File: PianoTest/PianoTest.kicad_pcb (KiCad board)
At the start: 4 copper layers, 120 x 90 mm, 199 parts, among them J101 SMA preampl., J102 SMA shaper, J301 TRIG est., J401 J_IN MAIN, J402 J_OUT MAIN, Q101 BF862, Q102 BF862, Q301 BSS138, U101 OPA4172ID, U102 ADS8326IDGKT, U103 TMP117AIDRVR, U201 MCP23S17-E/ML, U202 TMUX1112RSVR, U203 TMUX1112RSVR, U204 BGSA142GN12, U205 BGSA142GN12, U301 LTC6993CS6-2, U302 AD5245BRJZ100, U401 74HC283, U402 74HC85, U403 74HC138, U404 SN74LVC2G17DBVR, U405 SN74LVC1G125DBVR, U406 SN74LVC1G332DBVR, U407 SN74LVC1G07DBVR, U408 25AA02E48T-I/SN, U501 DAC61402RHBR, U502 INA239AIDGSR

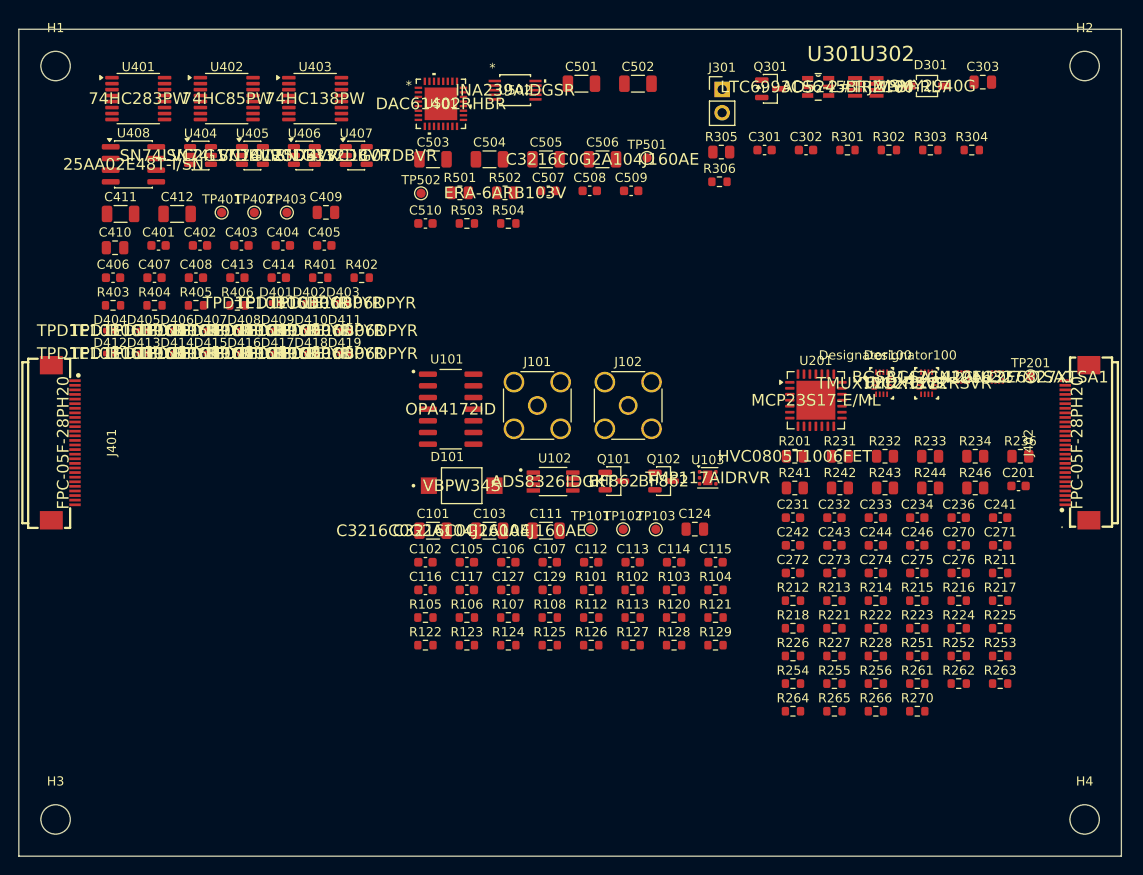
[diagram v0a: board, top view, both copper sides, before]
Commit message: PianoTest: discriminatore, latch e rilevatore di picco
Comparatore TLV3501 su SHAPER_OUT con soglia dal canale B del DAC61402
(partitore 22k/10k, BAT54S), latch 74LVC1G74 su GPA7 dell'MCP (ALERT#),
uscita HIT su TP e SMA. Rilevatore di picco OPA2365 + BAS416 + hold 1 nF
C0G prima dell'ADS8326, con reset da accesso SPI all'indirizzo 3 e
ponticello 0R per scavalcarlo. Trigger del LED dallo strobe dell'indirizzo 4.
Articolo: sezione 3.1 (formatore e acquisizione) aggiornata e ricompilata.
ERC 0.

Co-Authored-By: Claude Opus 5.5 (1M context) <noreply@anthropic.com>
Claude-Session: https://claude.ai/code/session_01J3krgWFTUEjwvCnwUp9cQn
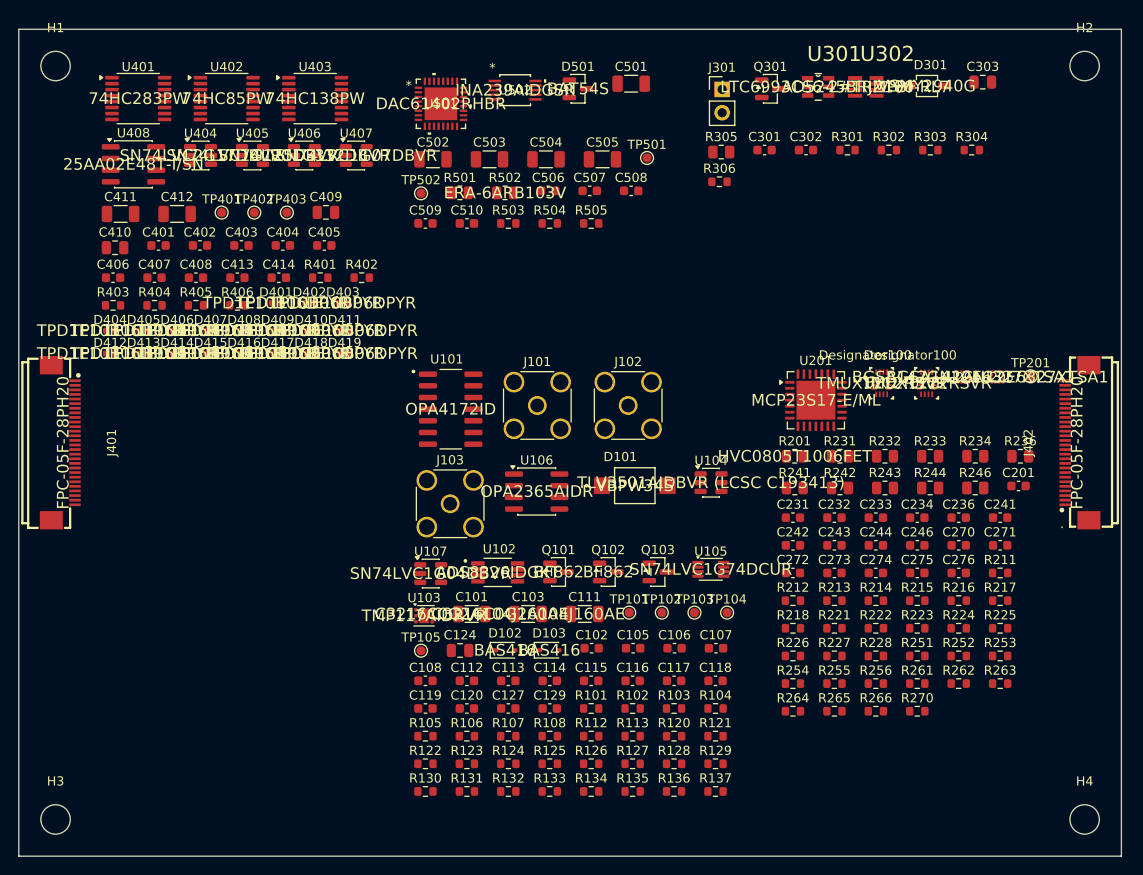
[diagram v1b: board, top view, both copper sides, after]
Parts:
- added C108: 1nF C0G, Capacitor_SMD:C_0603_1608Metric, F.Cu at (84.3, 110.9)
- added C118: 100nF, Capacitor_SMD:C_0603_1608Metric, F.Cu at (115.8, 110.9)
- added C119: 100nF, Capacitor_SMD:C_0603_1608Metric, F.Cu at (84.3, 113.9)
- added C120: 100nF, Capacitor_SMD:C_0603_1608Metric, F.Cu at (88.8, 113.9)
- added D102: BAS416, Diode_SMD:D_SOD-323, F.Cu at (92.9, 107.6)
- added D103: BAS416, Diode_SMD:D_SOD-323, F.Cu at (97.7, 107.6)
- added D501: BAT54S, Package_TO_SOT_SMD:SOT-23, F.Cu at (100.9, 46.5)
- added J103: SMA HIT, Connector_Coaxial:SMA_Amphenol_132134_Vertical, F.Cu at (86.9, 91.6)
- added Q103: BSS138, Package_TO_SOT_SMD:SOT-23, F.Cu at (109.6, 99.1)
- added R130: 1k, Resistor_SMD:R_0603_1608Metric, F.Cu at (84.3, 123.0)
- added R131: 1M, Resistor_SMD:R_0603_1608Metric, F.Cu at (88.8, 123.0)
- added R132: 1k, Resistor_SMD:R_0603_1608Metric, F.Cu at (93.3, 123.0)
- added R133: 10k, Resistor_SMD:R_0603_1608Metric, F.Cu at (97.8, 123.0)
- added R134: 100k, Resistor_SMD:R_0603_1608Metric, F.Cu at (102.3, 123.0)
- added R135: 0R, Resistor_SMD:R_0603_1608Metric, F.Cu at (106.8, 123.0)
- added R136: 0R, Resistor_SMD:R_0603_1608Metric, F.Cu at (111.3, 123.0)
- added R137: 100R, Resistor_SMD:R_0603_1608Metric, F.Cu at (115.8, 123.0)
- added R505: 10k, Resistor_SMD:R_0603_1608Metric, F.Cu at (102.3, 61.1)
- added TP104: HIT, TestPoint:TestPoint_Pad_D1.0mm, F.Cu at (117.1, 103.5)
- added TP105: PK_OUT, TestPoint:TestPoint_Pad_D1.0mm, F.Cu at (83.8, 107.6)
- added U104: TLV3501AIDBVR, Package_TO_SOT_SMD:SOT-23-6, F.Cu at (115.3, 89.3)
- added U105: SN74LVC1G74DCUR, Package_SO:VSSOP-8_2.3x2mm_P0.5mm, F.Cu at (115.3, 98.8)
- added U106: OPA2365AIDR, Package_SO:SOIC-8_3.9x4.9mm_P1.27mm, F.Cu at (96.4, 90.3)
- added U107: SN74LVC1G04DBVR, Package_TO_SOT_SMD:SOT-23-5, F.Cu at (84.8, 99.2)
- C506: value 100nF/100V C0G -> 100nF; footprint Capacitor_SMD:C_1206_3216Metric -> Capacitor_SMD:C_0603_1608Metric
- R503: value 1k -> 22k
- TP502: value VBIAS_B -> VTH
- moved U103 34.3 mm to (84.1, 103.8)
- moved C124 28.8 mm to (88.0, 107.6)
- moved C117 24.6 mm to (111.3, 110.9)
- moved C116 24.6 mm to (106.8, 110.9)
- moved C502 23.8 mm to (85.1, 54.2)
- moved C509 22.7 mm to (84.3, 61.1)
- moved C102 20.4 mm to (102.3, 107.4)
- moved C105 20.4 mm to (106.9, 107.4)
- moved C107 20.4 mm to (115.9, 107.4)
- moved C106 20.4 mm to (111.4, 107.4)
- moved D101 18.8 mm to (107.0, 89.7)
- moved C115 18.7 mm to (102.3, 110.9)
- moved C114 18.7 mm to (97.8, 110.9)
- moved C112 18.7 mm to (88.8, 110.9)
- moved C113 18.7 mm to (93.3, 110.9)
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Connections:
- net /BiasDiodo/VBIAS_B renamed VTH
- net /bus-pnp/CS_Y3 renamed CS_Y3
- R106 pad 1: /Rivelatore/SHAPER_OUT -> /Rivelatore/ADC_SRC
- R304 pad 1: TRIG_MCP -> CS_Y4
- TP402 pad 1: /bus-pnp/CS_Y4 -> CS_Y4
- U201 pad 24: TRIG_MCP -> HIT_LATCH
- U403 pad 11: /bus-pnp/CS_Y4 -> CS_Y4

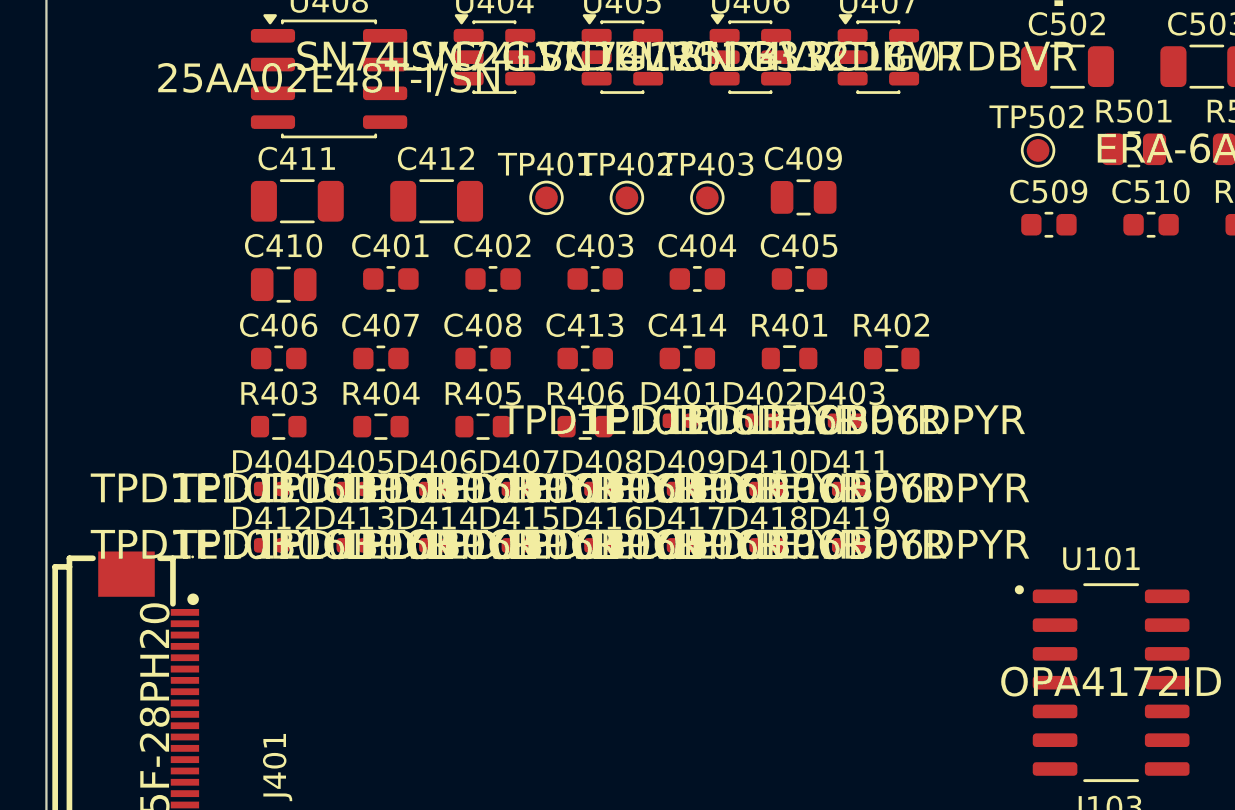
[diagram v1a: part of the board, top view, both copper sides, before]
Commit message: Bus MIKILAB REV5.1: linea di coincidenza HIT# sul pin 28 del MAIN
Specifica: pin 28 (prima GND ridondante) = HIT#, open-drain attivo basso,
pull-up unico 4.7k sul master, impulso 100-200 ns per evento; logica di
coincidenza documentata (fronte marcato dal master, lettura dei latch).
PianoTest: HIT -> monostabile 74LVC1G123 (2k + 27 pF) -> 74LVC1G06 su
HIT#, passante J_IN -> J_OUT, ESD. ERC 0.
SchedaA133: J2 pin 28 -> PD4 (PD_EINT4), pull-up R336 4.7k, ESD su U307,
R337 0R DNP verso l'EXTINT del NEO-F10T. ERC 0, PDF rigenerato.
Documentazione bus della A133 e articolo (sezione bus e coincidenze)
aggiornati; corretta l'identita del primo piano (0).

Co-Authored-By: Claude Opus 5.5 (1M context) <noreply@anthropic.com>
Claude-Session: https://claude.ai/code/session_01J3krgWFTUEjwvCnwUp9cQn
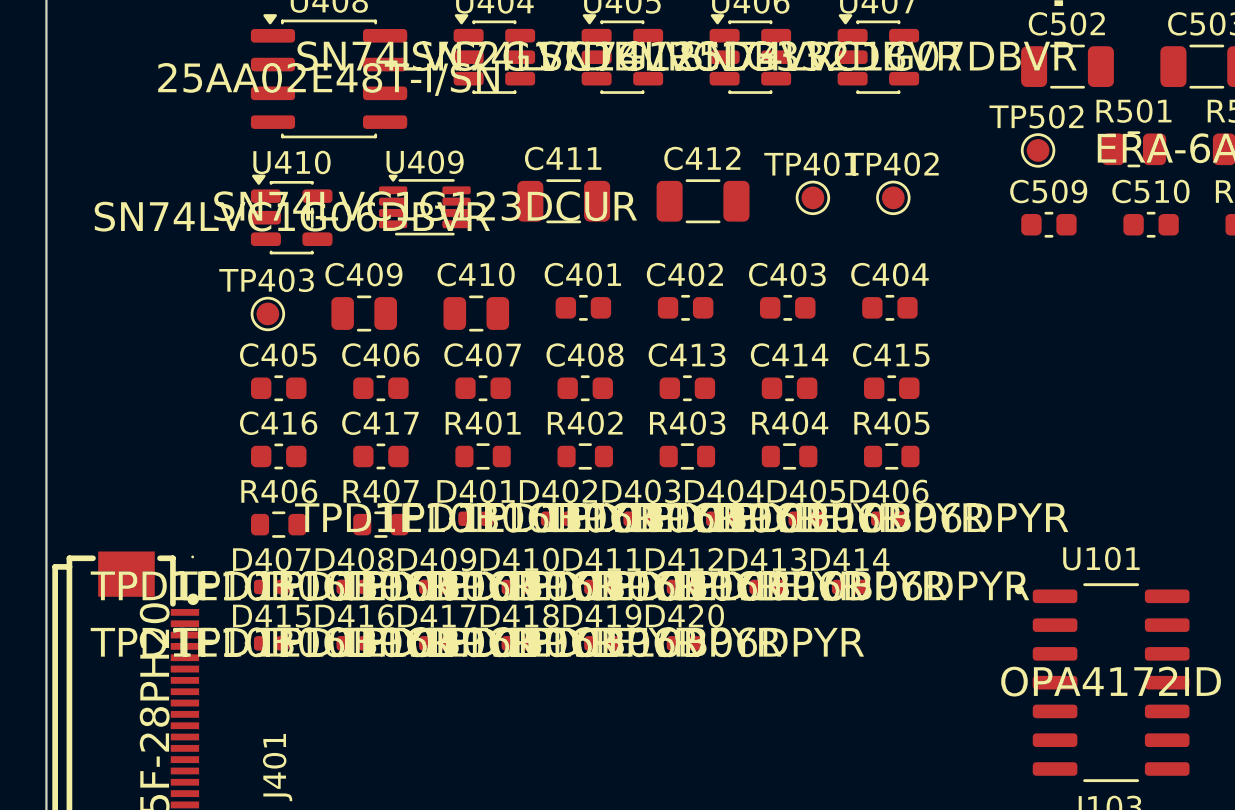
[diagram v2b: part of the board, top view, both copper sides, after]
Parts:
- added C415: 27pF C0G, Capacitor_SMD:C_0603_1608Metric, F.Cu at (77.3, 68.4)
- added C416: 100nF, Capacitor_SMD:C_0603_1608Metric, F.Cu at (50.3, 71.4)
- added C417: 100nF, Capacitor_SMD:C_0603_1608Metric, F.Cu at (54.8, 71.4)
- added D420: TPD1E10B06, Diode_SMD:D_0402_1005Metric, F.Cu at (68.2, 79.6)
- added R407: 2k, Resistor_SMD:R_0603_1608Metric, F.Cu at (54.8, 74.4)
- added U409: SN74LVC1G123DCUR, Package_SO:VSSOP-8_2.3x2mm_P0.5mm, F.Cu at (56.7, 60.4)
- added U410: SN74LVC1G06DBVR, Package_TO_SOT_SMD:SOT-23-5, F.Cu at (50.8, 60.8)
- moved C405 23.5 mm to (50.3, 68.4)
- moved C409 20.1 mm to (54.0, 65.1)
- moved TP403 20.1 mm to (49.8, 65.1)
- moved D405 20.0 mm to (73.5, 74.1)
- moved D404 20.0 mm to (69.9, 74.1)
- moved D406 20.0 mm to (77.2, 74.1)
- moved D412 18.3 mm to (68.2, 77.1)
- moved D413 18.3 mm to (71.8, 77.1)
- moved D414 18.3 mm to (75.5, 77.1)
- moved R403 18.1 mm to (68.3, 71.4)
- moved R404 18.1 mm to (72.8, 71.4)
- moved R405 18.1 mm to (77.3, 71.4)
- moved R406 14.2 mm to (50.3, 74.4)
- moved R401 14.2 mm to (59.3, 71.4)
- moved R402 14.2 mm to (63.8, 71.4)
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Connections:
- net /Rivelatore/HIT renamed HIT
- D414 pad 1: /bus-pnp/ID_IN0 -> /bus-pnp/BUS_HIT_N
- D415 pad 1: /bus-pnp/ID_IN1 -> /bus-pnp/ID_IN0
- D416 pad 1: /bus-pnp/ID_IN2 -> /bus-pnp/ID_IN1
- D417 pad 1: /bus-pnp/ID_OUT0 -> /bus-pnp/ID_IN2
- D418 pad 1: /bus-pnp/ID_OUT1 -> /bus-pnp/ID_OUT0
- D419 pad 1: /bus-pnp/ID_OUT2 -> /bus-pnp/ID_OUT1
- J401 pad 28: GND -> /bus-pnp/BUS_HIT_N
- J402 pad 28: GND -> /bus-pnp/BUS_HIT_N
